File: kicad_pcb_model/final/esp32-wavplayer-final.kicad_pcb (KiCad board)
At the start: 2 copper layers, 40 x 49.4 mm, 0 parts

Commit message: updating model
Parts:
- added A1: 3.5mmAudioJack, Connector_Audio:Jack_3.5mm_KoreanHropartsElec_PJ-320D-4A_Horizontal, F.Cu at (188.1, 59.5)
- added AC1: 0.1uF, Capacitor_SMD:C_0603_1608Metric_Pad1.08x0.95mm_HandSolder, F.Cu at (189.1, 34.0)
- added AC10: 0.1uF, Capacitor_SMD:C_0603_1608Metric_Pad1.08x0.95mm_HandSolder, F.Cu at (180.9, 45.2)
- added AC11: 2.2uF, Capacitor_SMD:C_0603_1608Metric_Pad1.08x0.95mm_HandSolder, F.Cu at (180.9, 47.7)
- added AC12: 2.2nF, Capacitor_SMD:C_0603_1608Metric_Pad1.08x0.95mm_HandSolder, F.Cu at (180.9, 50.2)
- added AC13: 2.2nF, Capacitor_SMD:C_0603_1608Metric_Pad1.08x0.95mm_HandSolder, F.Cu at (180.9, 52.7)
- added AC14: 2.2uF, Capacitor_SMD:C_0603_1608Metric_Pad1.08x0.95mm_HandSolder, F.Cu at (185.2, 38.0)
- added AC2: 10uF, Capacitor_SMD:C_0603_1608Metric_Pad1.08x0.95mm_HandSolder, F.Cu at (189.1, 36.5)
- added AC3: 0.1uF, Capacitor_SMD:C_0603_1608Metric_Pad1.08x0.95mm_HandSolder, F.Cu at (189.1, 39.0)
- added AC4: 0.1uF, Capacitor_SMD:C_0603_1608Metric_Pad1.08x0.95mm_HandSolder, F.Cu at (189.1, 41.5)
- added AC5: 10uF, Capacitor_SMD:C_0603_1608Metric_Pad1.08x0.95mm_HandSolder, F.Cu at (180.9, 32.7)
- added AC6: 0.1uF, Capacitor_SMD:C_0603_1608Metric_Pad1.08x0.95mm_HandSolder, F.Cu at (180.9, 35.2)
- added AC7: 10uF, Capacitor_SMD:C_0603_1608Metric_Pad1.08x0.95mm_HandSolder, F.Cu at (180.9, 37.7)
- added AC8: 0.1uF, Capacitor_SMD:C_0603_1608Metric_Pad1.08x0.95mm_HandSolder, F.Cu at (180.9, 40.2)
- added AC9: 10uF, Capacitor_SMD:C_0603_1608Metric_Pad1.08x0.95mm_HandSolder, F.Cu at (180.9, 42.7)
- added AD1: D, Diode_SMD:D_0603_1608Metric_Pad1.05x0.95mm_HandSolder, F.Cu at (191.4, 44.8)
- added AR1: 470, Resistor_SMD:R_0603_1608Metric_Pad0.98x0.95mm_HandSolder, F.Cu at (185.2, 40.5)
- added AR2: 470, Resistor_SMD:R_0603_1608Metric_Pad0.98x0.95mm_HandSolder, F.Cu at (185.2, 43.0)
- added AR3: 1k, Resistor_SMD:R_0603_1608Metric_Pad0.98x0.95mm_HandSolder, F.Cu at (185.2, 45.5)
- added AVR1: ME6211C33M5, Package_TO_SOT_SMD:SOT-23-5, F.Cu at (196.1, 41.3)
- added AVR2: ME6211C33M5, Package_TO_SOT_SMD:SOT-23-5, F.Cu at (196.1, 45.9)
- added BATPROT1: DW01A, Package_TO_SOT_SMD:SOT-23-6, F.Cu at (194.9, 95.6)
- added BB1: TPS63030DSK, Package_SON:WSON-10-1EP_2.5x2.5mm_P0.5mm_EP1.2x2mm, F.Cu at (200.0, 128.5)
- added BC1: 100nF, Capacitor_SMD:C_0603_1608Metric_Pad1.08x0.95mm_HandSolder, F.Cu at (125.9, 131.4)
- added BCC1: 0.1uF, Capacitor_SMD:C_0603_1608Metric_Pad1.08x0.95mm_HandSolder, F.Cu at (195.4, 128.0)
- added BCC2: 10uF, Capacitor_SMD:C_0603_1608Metric_Pad1.08x0.95mm_HandSolder, F.Cu at (195.4, 130.5)
- added BCC3: 10uF, Capacitor_SMD:C_0603_1608Metric_Pad1.08x0.95mm_HandSolder, F.Cu at (204.3, 128.5)
- added BCL1: 2.2uH, Inductor_SMD:L_0201_0603Metric_Pad0.64x0.40mm_HandSolder, F.Cu at (198.7, 131.4)
- added BCR1: 200k, Resistor_SMD:R_0603_1608Metric_Pad0.98x0.95mm_HandSolder, F.Cu at (204.3, 131.0)
- added BCR2: 1.2M, Resistor_SMD:R_0603_1608Metric_Pad0.98x0.95mm_HandSolder, F.Cu at (204.3, 133.5)
- added BD1: D, Diode_SMD:D_0603_1608Metric_Pad1.05x0.95mm_HandSolder, F.Cu at (141.3, 124.4)
- added BD2: D, Diode_SMD:D_0603_1608Metric_Pad1.05x0.95mm_HandSolder, F.Cu at (141.3, 127.0)
- added BMFT1: FS8205A, Package_TO_SOT_SMD:SOT-23-6, F.Cu at (194.9, 100.2)
- added BR1: 10k, Resistor_SMD:R_0603_1608Metric_Pad0.98x0.95mm_HandSolder, F.Cu at (141.6, 129.7)
- added BR2: 10k, Resistor_SMD:R_0603_1608Metric_Pad0.98x0.95mm_HandSolder, F.Cu at (141.6, 132.2)
- added BR3: 4.7k, Resistor_SMD:R_0603_1608Metric_Pad0.98x0.95mm_HandSolder, F.Cu at (141.6, 134.7)
- added BR4: 6.8k, Resistor_SMD:R_0603_1608Metric_Pad0.98x0.95mm_HandSolder, F.Cu at (129.7, 131.2)
- added BR5: 15k, Resistor_SMD:R_0603_1608Metric_Pad0.98x0.95mm_HandSolder, F.Cu at (129.7, 133.7)
- added BTM1: TP4056-42-ESOP8, Package_SO:SOIC-8_3.9x4.9mm_P1.27mm, F.Cu at (186.2, 92.8)
- added CC1: 1uF, Capacitor_SMD:C_0603_1608Metric_Pad1.08x0.95mm_HandSolder, F.Cu at (157.1, 123.0)
- added CC2: 1uF, Capacitor_SMD:C_0603_1608Metric_Pad1.08x0.95mm_HandSolder, F.Cu at (157.1, 125.5)
- added CC3: 100nF, Capacitor_SMD:C_0603_1608Metric_Pad1.08x0.95mm_HandSolder, F.Cu at (157.1, 128.0)
- added CC4: 100nF, Capacitor_SMD:C_0603_1608Metric_Pad1.08x0.95mm_HandSolder, F.Cu at (157.1, 130.5)
- added CC5: 1uF, Capacitor_SMD:C_0603_1608Metric_Pad1.08x0.95mm_HandSolder, F.Cu at (162.5, 129.8)
- added CC6: 10uF, Capacitor_SMD:C_0603_1608Metric_Pad1.08x0.95mm_HandSolder, F.Cu at (162.5, 132.3)
- added CC7: 1uF, Capacitor_SMD:C_0603_1608Metric_Pad1.08x0.95mm_HandSolder, F.Cu at (157.1, 132.8)
- added CC8: 10nF, Capacitor_SMD:C_0603_1608Metric_Pad1.08x0.95mm_HandSolder, F.Cu at (167.9, 124.0)
- added CC9: 10nF, Capacitor_SMD:C_0603_1608Metric_Pad1.08x0.95mm_HandSolder, F.Cu at (167.9, 126.5)
- added CPU1: ESP32-C3-H*, Package_DFN_QFN:QFN-32-1EP_5x5mm_P0.5mm_EP3.45x3.45mm, F.Cu at (162.8, 125.1)
- added CR1: 10k, Resistor_SMD:R_0603_1608Metric_Pad0.98x0.95mm_HandSolder, F.Cu at (167.9, 129.0)
- added CR2: 10k, Resistor_SMD:R_0603_1608Metric_Pad0.98x0.95mm_HandSolder, F.Cu at (167.9, 131.5)
- added CR3: 22R, Resistor_SMD:R_0603_1608Metric_Pad0.98x0.95mm_HandSolder, F.Cu at (189.3, 85.6)
- added CR4: 22R, Resistor_SMD:R_0603_1608Metric_Pad0.98x0.95mm_HandSolder, F.Cu at (189.3, 88.1)
- added CYOC1: 3225-40m, Oscillator:Oscillator_SMD_Abracon_ASE-4Pin_3.2x2.5mm, F.Cu at (164.9, 137.9)
- added D3: PWRLED, LED_SMD:LED_0603_1608Metric_Pad1.05x0.95mm_HandSolder, F.Cu at (130.4, 112.2)
- added D4: ONLED, LED_SMD:LED_0603_1608Metric_Pad1.05x0.95mm_HandSolder, F.Cu at (130.4, 114.8)
- added D5: CHRGLED, LED_SMD:LED_0603_1608Metric_Pad1.05x0.95mm_HandSolder, F.Cu at (194.0, 85.8)
- added D6: STNDLED, LED_SMD:LED_0603_1608Metric_Pad1.05x0.95mm_HandSolder, F.Cu at (194.0, 88.4)
- added DB1: MicroSDDebug, Connector_PinHeader_2.54mm:PinHeader_1x06_P2.54mm_Vertical, F.Cu at (170.8, 45.6)
- added DB2: DisplayDebug, Connector_PinHeader_2.54mm:PinHeader_1x04_P2.54mm_Vertical, F.Cu at (178.7, 128.2)
- added DB3: PCM5102aDebug, Connector_PinHeader_2.54mm:PinHeader_1x06_P2.54mm_Vertical, F.Cu at (196.5, 50.7)
- added DB4: DebugPinVbat, Connector_PinHeader_2.54mm:PinHeader_1x01_P2.54mm_Vertical, F.Cu at (190.8, 128.0)
- added DC1: 2.2uF, Capacitor_SMD:C_0603_1608Metric_Pad1.08x0.95mm_HandSolder, F.Cu at (194.6, 112.0)
- added DC3: 1uF, Capacitor_SMD:C_0603_1608Metric_Pad1.08x0.95mm_HandSolder, F.Cu at (194.6, 114.5)
- added DC4: 1uF, Capacitor_SMD:C_0603_1608Metric_Pad1.08x0.95mm_HandSolder, F.Cu at (198.9, 111.8)
- added DC5: 1uF, Capacitor_SMD:C_0603_1608Metric_Pad1.08x0.95mm_HandSolder, F.Cu at (198.9, 114.3)
- added DC6: 1uF, Capacitor_SMD:C_0603_1608Metric_Pad1.08x0.95mm_HandSolder, F.Cu at (198.9, 116.8)
- added DC7: 4.7uF, Capacitor_SMD:C_0603_1608Metric_Pad1.08x0.95mm_HandSolder, F.Cu at (190.7, 112.0)
- added DQ1: FDN338P, Package_TO_SOT_SMD:SOT-23, F.Cu at (177.7, 111.0)
- added DQ2: FDN335N, Package_TO_SOT_SMD:SOT-23, F.Cu at (177.7, 115.4)
- added DR1: 4.7k, Resistor_SMD:R_0603_1608Metric_Pad0.98x0.95mm_HandSolder, F.Cu at (190.7, 114.5)
- added DR2: 4.7k, Resistor_SMD:R_0603_1608Metric_Pad0.98x0.95mm_HandSolder, F.Cu at (182.9, 112.2)
- added DR3: 620k, Resistor_SMD:R_0603_1608Metric_Pad0.98x0.95mm_HandSolder, F.Cu at (186.6, 112.5)
- added DR4: 47k, Resistor_SMD:R_0603_1608Metric_Pad0.98x0.95mm_HandSolder, F.Cu at (186.6, 115.0)
- added DR5: 47k, Resistor_SMD:R_0603_1608Metric_Pad0.98x0.95mm_HandSolder, F.Cu at (182.9, 115.0)
- added DS1: Wisevision X096-2864KSWPG01-H30, Display:OLED-128O064D, F.Cu at (188.6, 123.2)
- added J1: BIN+, Connector_PinHeader_2.54mm:PinHeader_1x01_P2.54mm_Vertical, F.Cu at (193.8, 77.1)
- added J2: BIN-, Connector_PinHeader_2.54mm:PinHeader_1x01_P2.54mm_Vertical, F.Cu at (193.8, 81.7)
- added LR1: 5.1k, Resistor_SMD:R_0603_1608Metric_Pad0.98x0.95mm_HandSolder, F.Cu at (130.3, 106.7)
- added LR2: 5.1k, Resistor_SMD:R_0603_1608Metric_Pad0.98x0.95mm_HandSolder, F.Cu at (130.3, 109.2)
- added MSD1: Generic MicroSD, Connector_Card:microSD_HC_Hirose_DM3AT-SF-PEJM5, F.Cu at (160.9, 51.2)
- added OC2: 15pF, Capacitor_SMD:C_0603_1608Metric_Pad1.08x0.95mm_HandSolder, F.Cu at (159.9, 136.8)
- added OC3: 15pF, Capacitor_SMD:C_0603_1608Metric_Pad1.08x0.95mm_HandSolder, F.Cu at (159.9, 139.3)
- added PC1: 10uF, Capacitor_SMD:C_0603_1608Metric_Pad1.08x0.95mm_HandSolder, F.Cu at (181.6, 85.6)
- added PC2: 10uF, Capacitor_SMD:C_0603_1608Metric_Pad1.08x0.95mm_HandSolder, F.Cu at (181.6, 88.1)
- added PC3: 10uF, Capacitor_SMD:C_0603_1608Metric_Pad1.08x0.95mm_HandSolder, F.Cu at (185.4, 73.1)
- added PC4: 100nF, Capacitor_SMD:C_0603_1608Metric_Pad1.08x0.95mm_HandSolder, F.Cu at (185.4, 75.6)
- added PC5: 10uF, Capacitor_SMD:C_0603_1608Metric_Pad1.08x0.95mm_HandSolder, F.Cu at (185.4, 78.1)
- added PD1: D, Diode_SMD:D_0603_1608Metric_Pad1.05x0.95mm_HandSolder, F.Cu at (194.0, 91.0)
- added PDVR1: ME6211C33M5, Package_TO_SOT_SMD:SOT-23-5, F.Cu at (194.9, 104.8)
- added PR1: 5.1K, Resistor_SMD:R_0603_1608Metric_Pad0.98x0.95mm_HandSolder, F.Cu at (185.4, 80.6)
- added PR2: 5.1K, Resistor_SMD:R_0603_1608Metric_Pad0.98x0.95mm_HandSolder, F.Cu at (185.4, 83.2)
- added PR3: 0.4, Resistor_SMD:R_0603_1608Metric_Pad0.98x0.95mm_HandSolder, F.Cu at (185.4, 85.7)
- added PR4: 1k, Resistor_SMD:R_0603_1608Metric_Pad0.98x0.95mm_HandSolder, F.Cu at (185.4, 88.2)
- added PR5: 1k, Resistor_SMD:R_0603_1608Metric_Pad0.98x0.95mm_HandSolder, F.Cu at (189.5, 75.3)
- added PR6: 1k, Resistor_SMD:R_0603_1608Metric_Pad0.98x0.95mm_HandSolder, F.Cu at (189.5, 77.8)
- added PR7: 100, Resistor_SMD:R_0603_1608Metric_Pad0.98x0.95mm_HandSolder, F.Cu at (189.5, 80.3)
- added PR8: 1K, Resistor_SMD:R_0603_1608Metric_Pad0.98x0.95mm_HandSolder, F.Cu at (189.5, 82.9)
- added SC1: 100nF, Capacitor_SMD:C_0603_1608Metric_Pad1.08x0.95mm_HandSolder, F.Cu at (150.7, 44.1)
- added SC2: 10nF, Capacitor_SMD:C_0603_1608Metric_Pad1.08x0.95mm_HandSolder, F.Cu at (150.7, 46.6)
- added SR1: 10k, Resistor_SMD:R_0603_1608Metric_Pad0.98x0.95mm_HandSolder, F.Cu at (150.7, 49.1)
- added SR2: 10k, Resistor_SMD:R_0603_1608Metric_Pad0.98x0.95mm_HandSolder, F.Cu at (150.7, 51.6)
- added SR3: 10k, Resistor_SMD:R_0603_1608Metric_Pad0.98x0.95mm_HandSolder, F.Cu at (150.7, 54.1)
- added SR4: 10k, Resistor_SMD:R_0603_1608Metric_Pad0.98x0.95mm_HandSolder, F.Cu at (150.7, 56.6)
- added SW1: RST, Button_Switch_SMD:SW_SPST_TS-1088-xR020, F.Cu at (135.5, 122.8)
- added SW2: BOOT/UP, Button_Switch_SMD:SW_SPST_TS-1088-xR020, F.Cu at (135.5, 127.3)
- added SW3: RIGHT, Button_Switch_SMD:SW_SPST_TS-1088-xR020, F.Cu at (135.5, 131.8)
- added SW4: LEFT, Button_Switch_SMD:SW_SPST_TS-1088-xR020, F.Cu at (128.7, 123.2)
- added SW5: DOWN, Button_Switch_SMD:SW_SPST_TS-1088-xR020, F.Cu at (128.7, 127.8)
- added U3: PCM5102A, Package_SO:TSSOP-20_4.4x6.5mm_P0.65mm, F.Cu at (189.1, 50.4)
- added USB1: USBC-6Pin, Connector_USB:USB_C_Receptacle_HRO_TYPE-C-31-M-12, F.Cu at (187.0, 102.6)

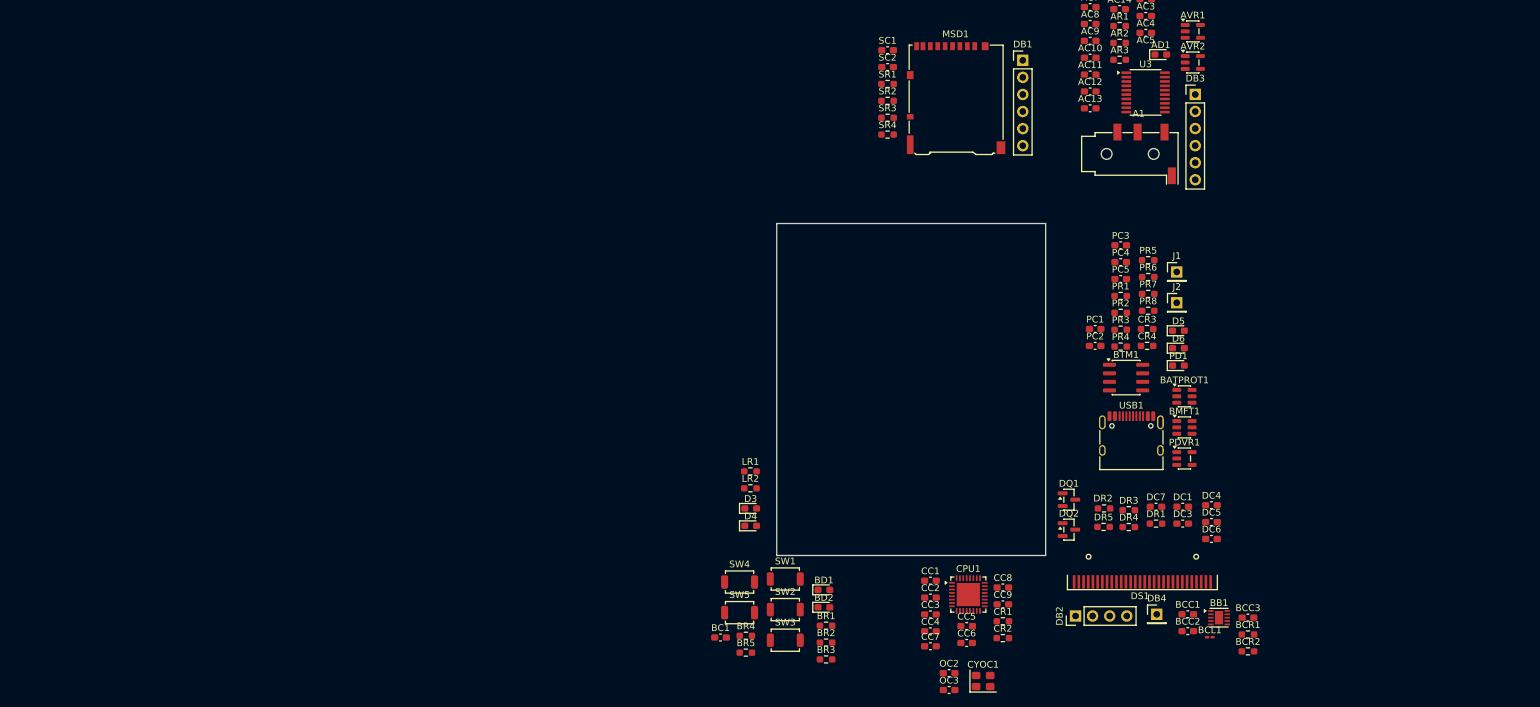
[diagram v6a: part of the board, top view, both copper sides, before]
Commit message: fixed battery connection
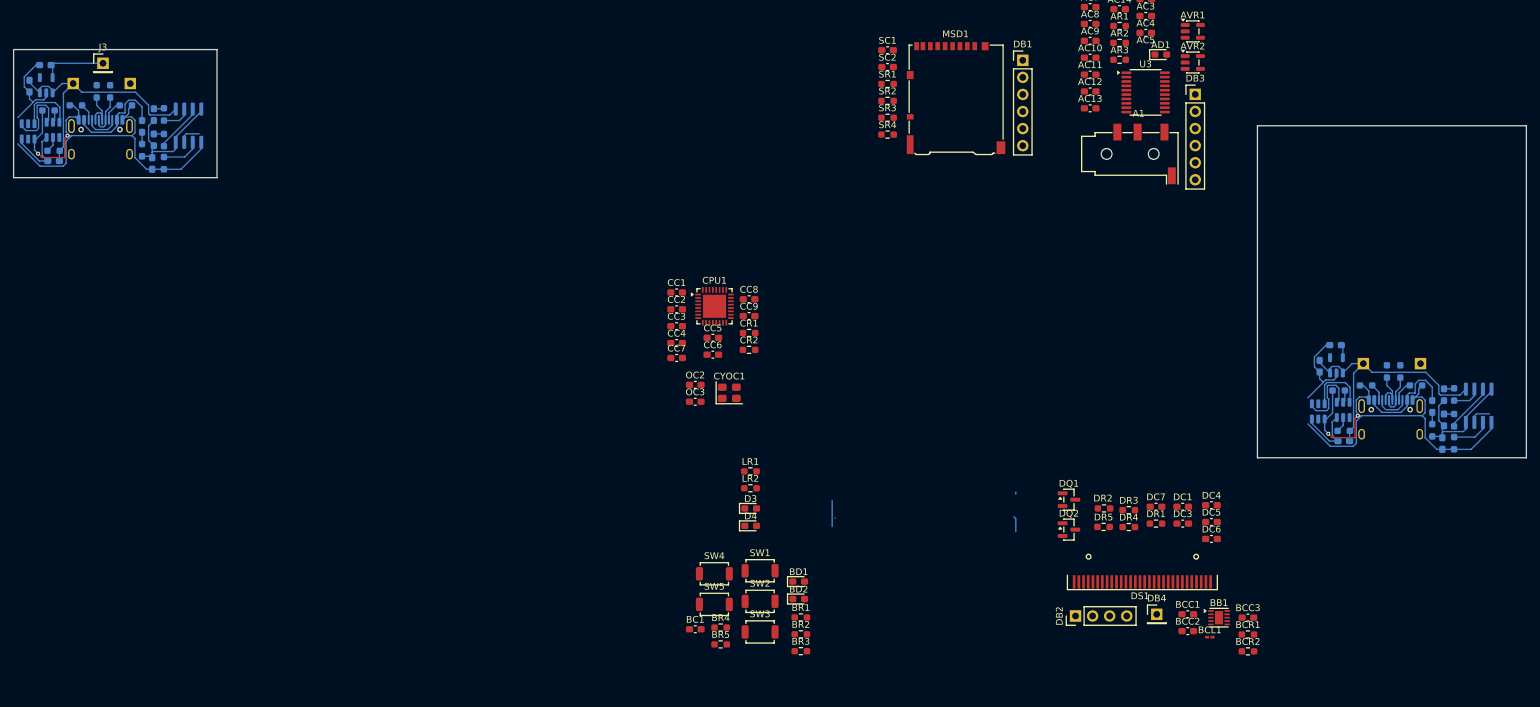
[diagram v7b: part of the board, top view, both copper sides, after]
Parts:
- removed PC5: 10uF, Capacitor_SMD:C_0603_1608Metric_Pad1.08x0.95mm_HandSolder
- added BATPROT1: DW01A, Package_TO_SOT_SMD:SOT-23-6, B.Cu at (26.6, 55.9)
- added BMFT1: FS8205A, Package_TO_SOT_SMD:SOT-23-6, B.Cu at (22.9, 56.2)
- added BTM1: TP4056-42-ESOP8, Package_SO:SOIC-8_3.9x4.9mm_P1.27mm, B.Cu at (46.8, 55.3)
- added CR3: 22R, Resistor_SMD:R_0603_1608Metric_Pad0.98x0.95mm_HandSolder, B.Cu at (35.1, 50.2)
- added CR4: 22R, Resistor_SMD:R_0603_1608Metric_Pad0.98x0.95mm_HandSolder, B.Cu at (33.1, 50.2)
- added D5: CHRGLED, LED_SMD:LED_0603_1608Metric_Pad1.05x0.95mm_HandSolder, B.Cu at (41.6, 57.4)
- added D6: STNDLED, LED_SMD:LED_0603_1608Metric_Pad1.05x0.95mm_HandSolder, B.Cu at (41.6, 53.7)
- added J1: BIN+, Connector_PinHeader_2.54mm:PinHeader_1x01_P2.54mm_Vertical, B.Cu at (29.6, 49.1)
- added J2: BIN-, Connector_PinHeader_2.54mm:PinHeader_1x01_P2.54mm_Vertical, B.Cu at (38.1, 49.1)
- added J3: DBG3v3, Connector_PinHeader_2.54mm:PinHeader_1x01_P2.54mm_Vertical, F.Cu at (34.0, 46.0)
- added PC1: 10uF, Capacitor_SMD:C_0603_1608Metric_Pad1.08x0.95mm_HandSolder, B.Cu at (23.1, 49.4)
- added PC2: 10uF, Capacitor_SMD:C_0603_1608Metric_Pad1.08x0.95mm_HandSolder, B.Cu at (25.5, 46.3)
- added PC3: 10uF, Capacitor_SMD:C_0603_1608Metric_Pad1.08x0.95mm_HandSolder, B.Cu at (41.4, 60.9)
- added PC4: 100nF, Capacitor_SMD:C_0603_1608Metric_Pad1.08x0.95mm_HandSolder, B.Cu at (26.7, 60.6)
- added PD1: D, Diode_SMD:D_0603_1608Metric_Pad1.05x0.95mm_HandSolder, B.Cu at (39.9, 55.4)
- added PDVR1: ME6211C33M5, Package_TO_SOT_SMD:SOT-23-5, B.Cu at (25.6, 49.3)
- added PR1: 5.1K, Resistor_SMD:R_0603_1608Metric_Pad0.98x0.95mm_HandSolder, B.Cu at (30.0, 52.3)
- added PR2: 5.1K, Resistor_SMD:R_0603_1608Metric_Pad0.98x0.95mm_HandSolder, B.Cu at (37.4, 52.3)
- added PR3: 0.4, Resistor_SMD:R_0603_1608Metric_Pad0.98x0.95mm_HandSolder, B.Cu at (39.9, 59.0)
- added PR4: 1k, Resistor_SMD:R_0603_1608Metric_Pad0.98x0.95mm_HandSolder, B.Cu at (43.1, 53.6)
- added PR5: 1k, Resistor_SMD:R_0603_1608Metric_Pad0.98x0.95mm_HandSolder, B.Cu at (43.1, 57.5)
- added PR6: 1k, Resistor_SMD:R_0603_1608Metric_Pad0.98x0.95mm_HandSolder, B.Cu at (43.1, 60.9)
- added PR7: 100, Resistor_SMD:R_0603_1608Metric_Pad0.98x0.95mm_HandSolder, B.Cu at (26.7, 59.1)
- added PR8: 1K, Resistor_SMD:R_0603_1608Metric_Pad0.98x0.95mm_HandSolder, B.Cu at (25.9, 53.1)
- added USB1: USBC-6Pin, Connector_USB:USB_C_Receptacle_HRO_TYPE-C-31-M-12, B.Cu at (33.7, 58.5)
- BATPROT1, BMFT1, BTM1, CR3, CR4, D5, D6, J1, J2, PC1, PC2, PC3, PC4, PD1, PDVR1, PR1, PR2, PR3, PR4, PR5, PR6, PR7, PR8, USB1: moved to B.Cu
- moved CC3 57.1 mm to (119.4, 85.1)
- moved CC1 57.1 mm to (119.4, 80.1)
- moved CC2 57.1 mm to (119.4, 82.6)
- moved CC4 57.1 mm to (119.4, 87.7)
- moved CC7 57.1 mm to (119.4, 89.9)
- moved CC5 57.1 mm to (124.8, 86.9)
- moved CC8 57.1 mm to (130.1, 81.1)
- moved CC9 57.1 mm to (130.1, 83.6)
- moved CPU1 57.1 mm to (125.0, 82.2)
- moved CR1 57.1 mm to (130.1, 86.2)
- moved CYOC1 57.1 mm to (127.2, 95.0)
- moved CC6 57.1 mm to (124.8, 89.4)
- moved CR2 57.1 mm to (130.1, 88.7)
- moved OC2 57.1 mm to (122.1, 93.9)
- moved OC3 57.1 mm to (122.1, 96.4)
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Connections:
- PC1 pad 1: Net-(PDVR1-CE) -> Net-(BTM1-BAT)
- PDVR1 pad 1: Net-(PDVR1-CE) -> Net-(BTM1-BAT)
- PDVR1 pad 3: Net-(PDVR1-CE) -> Net-(BTM1-BAT)
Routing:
- net Earth: track 0.00 -> 177.3 mm, vias 0 -> 4
- net Net-(BTM1-BAT): track 0.00 -> 80.1 mm
- net Net-(BTM1-CE): track 0.00 -> 37.8 mm
- net Net-(PD1-A): track 0.00 -> 31.9 mm
- net Net-(BATPROT1-OD): track 0.00 -> 21.7 mm
- net Net-(BATPROT1-GND): track 0.00 -> 20.9 mm
- net Net-(BATPROT1-OC): track 0.00 -> 18.6 mm
- net Net-(BTM1-~{CHRG}): track 0.00 -> 14.6 mm
- net Net-(CR4-Pad2): track 0.00 -> 12.8 mm
- net Net-(CR3-Pad2): track 0.00 -> 12.7 mm
- net +3V3: track 0.00 -> 11.7 mm
- net Net-(BTM1-PROG): track 0.00 -> 11.5 mm
- net (no net): track 0.00 -> 10.4 mm
- net Net-(BTM1-~{STDBY}): track 0.00 -> 8.59 mm
- net Net-(USB1-CC1): track 0.00 -> 6.21 mm
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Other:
- board size 40 x 49.4 mm -> 225 x 60.7 mm

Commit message: Added CPU board
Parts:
- removed the BATPROT1 at (26.6, 55.9)
- removed the BMFT1 at (22.9, 56.2)
- removed the BTM1 at (46.8, 55.3)
- removed the CR3 at (35.1, 50.2)
- removed the CR4 at (33.1, 50.2)
- removed the D5 at (41.6, 57.4)
- removed the D6 at (41.6, 53.7)
- removed J1: BIN+, Connector_PinHeader_2.54mm:PinHeader_1x01_P2.54mm_Vertical
- removed J2: BIN-, Connector_PinHeader_2.54mm:PinHeader_1x01_P2.54mm_Vertical
- removed the PC1 at (23.1, 49.4)
- removed the PC2 at (25.5, 46.3)
- removed the PC3 at (41.4, 60.9)
- removed the PC4 at (26.7, 60.6)
- removed the PD1 at (39.9, 55.4)
- removed the PDVR1 at (25.6, 49.3)
- removed the PR1 at (30.0, 52.3)
- removed the PR2 at (37.4, 52.3)
- removed the PR3 at (39.9, 59.0)
- removed the PR4 at (43.1, 53.6)
- removed the PR5 at (43.1, 57.5)
- removed the PR6 at (43.1, 60.9)
- removed the PR7 at (26.7, 59.1)
- removed the PR8 at (25.9, 53.1)
- removed the USB1 at (33.7, 58.5)
- added ?: , , F.Cu at (254.5, 95.0)
- added REF**: PinHeader_1x02_P2.54mm_Vertical, Connector_PinHeader_2.54mm:PinHeader_1x02_P2.54mm_Vertical, F.Cu at (268.5, 112.5)
- added REF**: PinHeader_1x02_P2.54mm_Vertical, Connector_PinHeader_2.54mm:PinHeader_1x02_P2.54mm_Vertical, F.Cu at (253.0, 97.5)
- added REF**: PinHeader_1x01_P2.54mm_Vertical, Connector_PinHeader_2.54mm:PinHeader_1x01_P2.54mm_Vertical, F.Cu at (262.0, 105.0)
- CC1, CC2, CC3, CC4, CC5, CC6, CC7, CC8, CC9, CPU1, CR1, CR2, CYOC1, OC2, OC3: moved to B.Cu
- moved J3 236.2 mm to (260.6, 112.7)
- moved CC3 149.2 mm to (267.9, 99.5), turned to 180 degrees
- moved CC7 148.4 mm to (267.2, 103.5)
- moved CC4 143.9 mm to (263.0, 95.3), turned to 90 degrees
- moved CC1 139.3 mm to (257.4, 98.5), turned to 180 degrees
- moved CC2 139.1 mm to (257.4, 100.0), turned to 180 degrees
- moved CPU1 138.9 mm to (262.8, 100.2), turned to -90 degrees
- moved CR1 138.4 mm to (267.7, 101.0)
- moved OC3 137.4 mm to (259.3, 104.6), turned to -90 degrees
- moved CC8 137.1 mm to (264.9, 106.5)
- moved CC5 137.0 mm to (261.5, 95.3), turned to 90 degrees
- moved CC9 136.4 mm to (264.9, 105.0)
- moved CC6 135.4 mm to (260.0, 95.3), turned to 90 degrees
- moved CR2 134.6 mm to (264.5, 95.4), turned to 90 degrees
- moved OC2 132.3 mm to (254.0, 104.1), turned to -90 degrees
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- renumbered J1 to +, J2 to -
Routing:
- net +3V3: track 11.7 -> 72.2 mm
- net Net-(BTM1-BAT): track 80.1 -> 40.1 mm
- net Earth: track 177.3 -> 156.1 mm, vias 4 -> 14
- net /GPIO18/USB_D+: track 0.00 -> 20.9 mm, vias 0 -> 1
- net /GPIO19/USB_D-: track 0.00 -> 19.1 mm, vias 0 -> 1
- net Net-(BTM1-CE): track 37.8 -> 19.1 mm
- net Net-(PD1-A): track 31.9 -> 16.0 mm
- net /XTAL_P: track 0.00 -> 10.9 mm
- net Net-(BATPROT1-OD): track 21.7 -> 10.9 mm
- net Net-(BATPROT1-GND): track 20.9 -> 10.5 mm
- net Net-(BATPROT1-OC): track 18.6 -> 9.30 mm
- net Net-(BTM1-~{CHRG}): track 14.6 -> 7.30 mm
- net /XTAL_N: track 0.00 -> 6.71 mm
- net Net-(CR4-Pad2): track 12.8 -> 6.41 mm
- net Net-(CR3-Pad2): track 12.7 -> 6.35 mm
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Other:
- board size 225 x 60.7 mm -> 29 x 37 mm
- board text added: "-"
- board text added: "3v"
- board text added: "D+-"
